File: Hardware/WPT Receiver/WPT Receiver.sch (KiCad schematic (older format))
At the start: 157 parts, among them J1 0.1\" Header, J2 Tag-connect-NL, J3 0.1\" Header, J4 0.1\" Header, SW1 PTS647, SW2 PTS647, SW3 PTS647, U1 STM32G031C6U6, U10 74HC595, U2 INA180A3, U3 MCP16331, U4 74HC595, U5 74HC595, U6 LM75B, U7 AH3574-P, U8 74HC595, U9 74HC595, Y1 8MHz

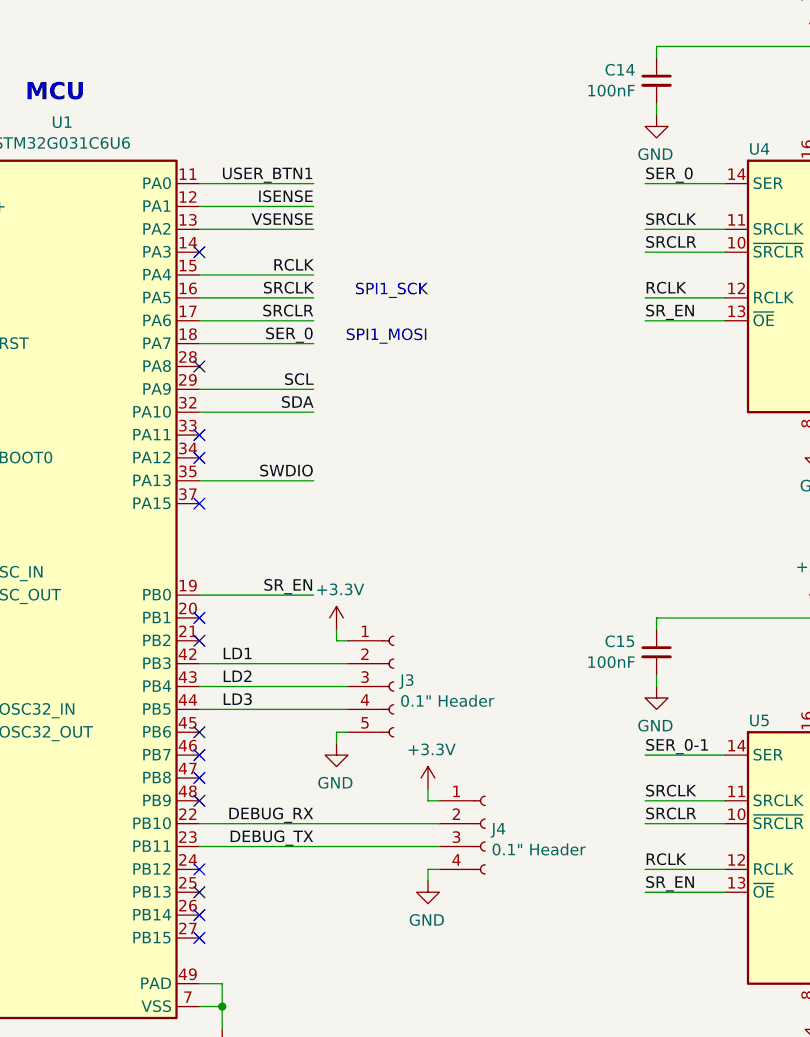
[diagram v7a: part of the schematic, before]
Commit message: Positioned non-power components, and routed most signals for peripherals other than shift regs/drivers. Added folder for 3D models for switch and crystal
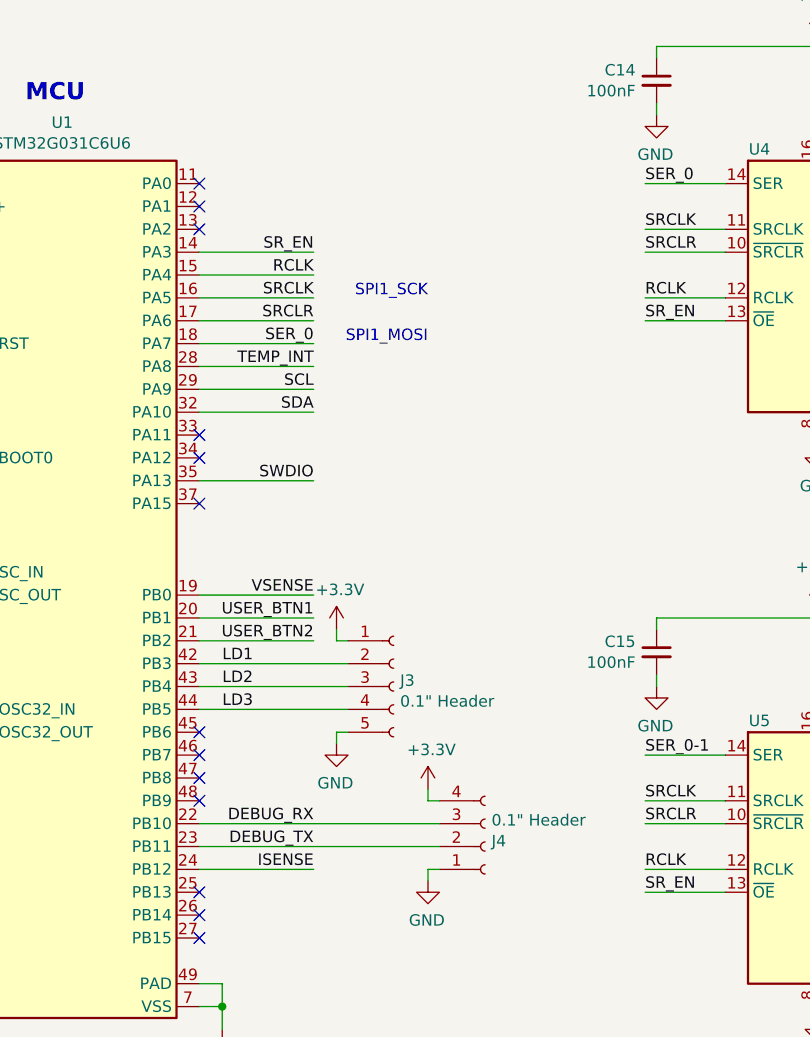
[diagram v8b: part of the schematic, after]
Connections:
- net +3V3: now also J4.4 (Pin_4); no longer J4.1 (Pin_1)
- net DEBUG_RX: now also J4.3 (Pin_3); no longer J4.2 (Pin_2)
- net DEBUG_TX: now also J4.2 (Pin_2); no longer J4.3 (Pin_3)
- net GND: now also J4.1 (Pin_1); no longer J4.4 (Pin_4)
- net ISENSE: now also U1.24 (PB12); no longer U1.12 (PA1)
- net SR_EN: now also U1.14 (PA3); no longer U1.19 (PB0)
- net TEMP_INT: now also U1.28 (PA8)
- net USER_BTN1: now also U1.20 (PB1); no longer U1.11 (PA0)
- net USER_BTN2: now also U1.21 (PB2)
- net VSENSE: now also U1.19 (PB0); no longer U1.13 (PA2)
- no-connect marks 24 -> 22
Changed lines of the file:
@@
 	3300 9650 3750 9650
 NoConn ~ 3300 9750
-Text Label 4100 5200 2    50   ~ 0
+Text Label 4100 8100 2    50   ~ 0
 ISENSE
-Text Label 4100 5300 2    50   ~ 0
+Text Label 4100 6900 2    50   ~ 0
 VSENSE
-Text Label 4100 5100 2    50   ~ 0
+Text Label 4100 7000 2    50   ~ 0
 USER_BTN1
 Text Notes 4600 5600 2    50   ~ 0
@@
 Text Label 4100 5800 2    50   ~ 0
 SER_0
-Text Label 4100 6900 2    50   ~ 0
+Text Label 4100 5400 2    50   ~ 0
 SR_EN
 Text Label 4100 7900 2    50   ~ 0
@@
 HALL_INT
 Wire Wire Line
-	4100 5100 3600 5100
-Wire Wire Line
-	3600 5200 4100 5200
-Wire Wire Line
-	3600 5300 4100 5300
-Wire Wire Line
 	3600 5500 4100 5500
 Wire Wire Line
@@
 Wire Wire Line
 	3600 6100 4100 6100
-Wire Wire Line
-	3600 6900 4100 6900
 Text Label 1550 5700 0    50   ~ 0
 RST
@@
 Text Notes 13300 2000 2    75   ~ 15
 SHIFT REGISTERS
-NoConn ~ 3600 5400
-NoConn ~ 3600 5900
+NoConn ~ 3600 5300
 NoConn ~ 3600 6200
 NoConn ~ 3600 6300
 NoConn ~ 3600 6500
-NoConn ~ 3600 7000
-NoConn ~ 3600 7100
+NoConn ~ 3600 5100
 NoConn ~ 3600 7500
 NoConn ~ 3600 7600
 NoConn ~ 3600 7700
 NoConn ~ 3600 7800
-NoConn ~ 3600 8100
 NoConn ~ 3600 8200
 NoConn ~ 3600 8300
@@
 NoConn ~ 2400 8000
 NoConn ~ 2400 7900
-NoConn ~ 2400 7800
 NoConn ~ 2400 7500
 NoConn ~ 2400 7400
@@
 L Connector:Conn_01x04_Female J4
 U 1 1 62243BA4
-P 4850 7900
-F 0 "J4" H 4878 7876 50  0000 L CNN
-F 1 "0.1\" Header" H 4878 7785 50  0000 L CNN
-F 2 "Connector_PinHeader_2.54mm:PinHeader_1x04_P2.54mm_Vertical" H 4850 7900 50  0001 C CNN
-F 3 "~" H 4850 7900 50  0001 C CNN
-	1    4850 7900
-	1    0    0    -1
+P 4850 8000
+F 0 "J4" H 4878 7976 50  0000 L CNN
+F 1 "0.1\" Header" H 4878 7885 50  0000 L CNN
+F 2 "Connector_PinHeader_2.54mm:PinHeader_1x04_P2.54mm_Vertical" H 4850 8000 50  0001 C CNN
+F 3 "~" H 4850 8000 50  0001 C CNN
+	1    4850 8000
+	1    0    0    1
 $EndComp
 $Comp
@@
 Wire Wire Line
 	8500 9500 8500 9600
+Wire Wire Line
+	3600 7000 4100 7000
+Text Label 4100 7100 2    50   ~ 0
+USER_BTN2
+Wire Wire Line
+	3600 7100 4100 7100
+Text Label 4100 5900 2    50   ~ 0
+TEMP_INT
+Wire Wire Line
+	4100 5900 3600 5900
+NoConn ~ 2400 7800
+Wire Wire Line
+	4100 5400 3600 5400
+Wire Wire Line
+	4100 6900 3600 6900
+Wire Wire Line
+	3600 8100 4100 8100
+NoConn ~ 3600 5200
 $EndSCHEMATC
